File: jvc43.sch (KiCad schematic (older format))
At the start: 0 parts

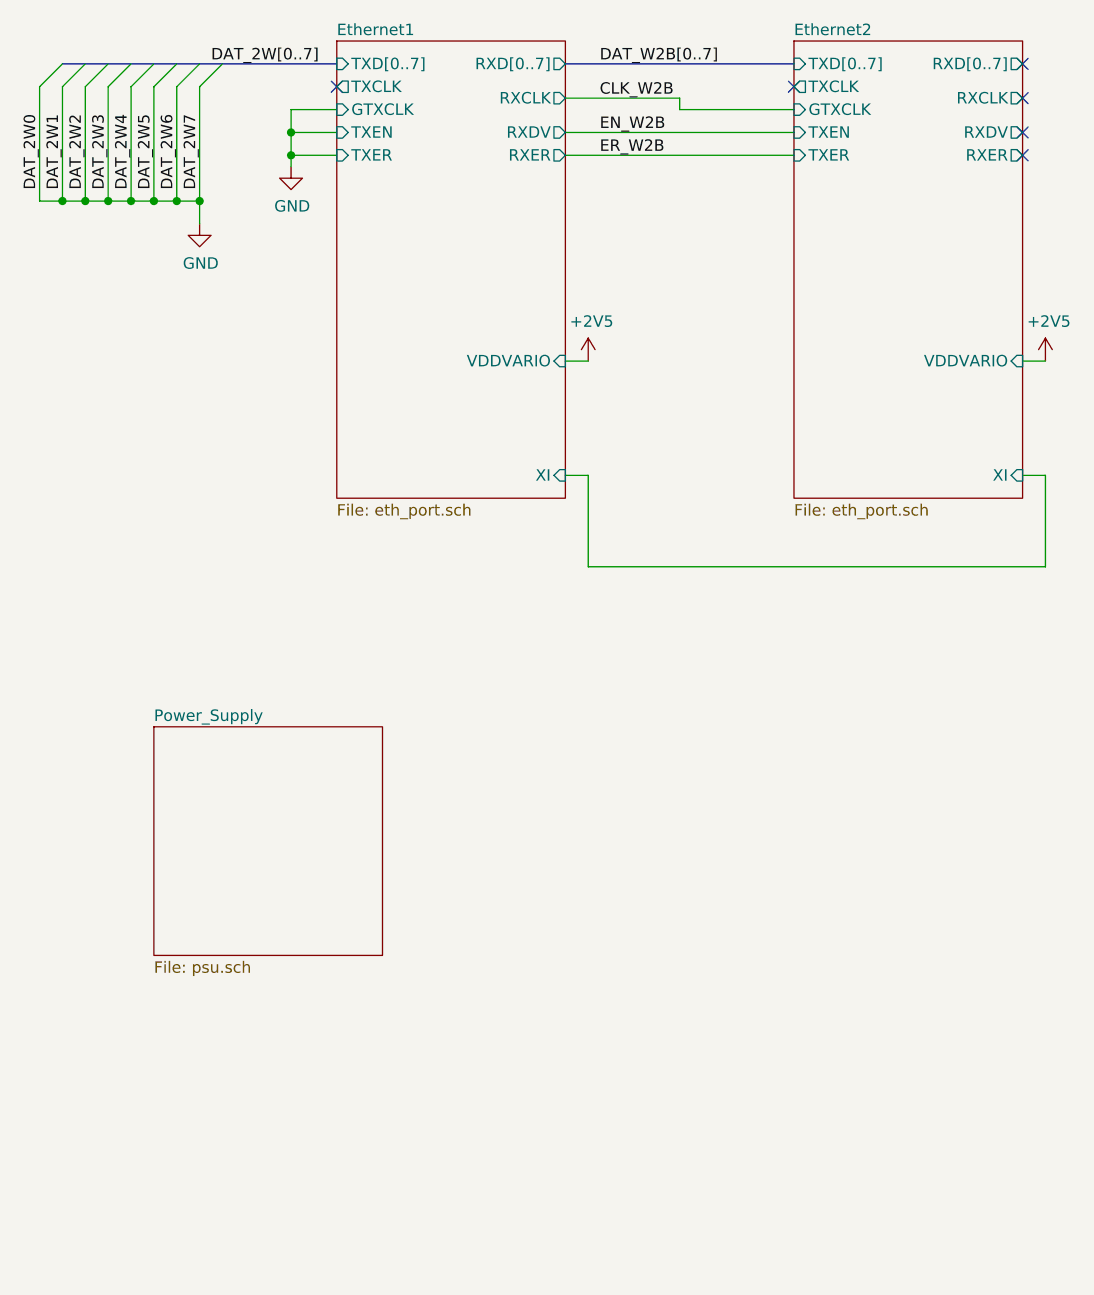
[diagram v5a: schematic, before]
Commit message: - Selected, schematic'd, placed & routed a crystal oscillator - Filled various internal planes to even out board thickness as well as   improve EMI performance - Added some identifying text to the top silkscreen
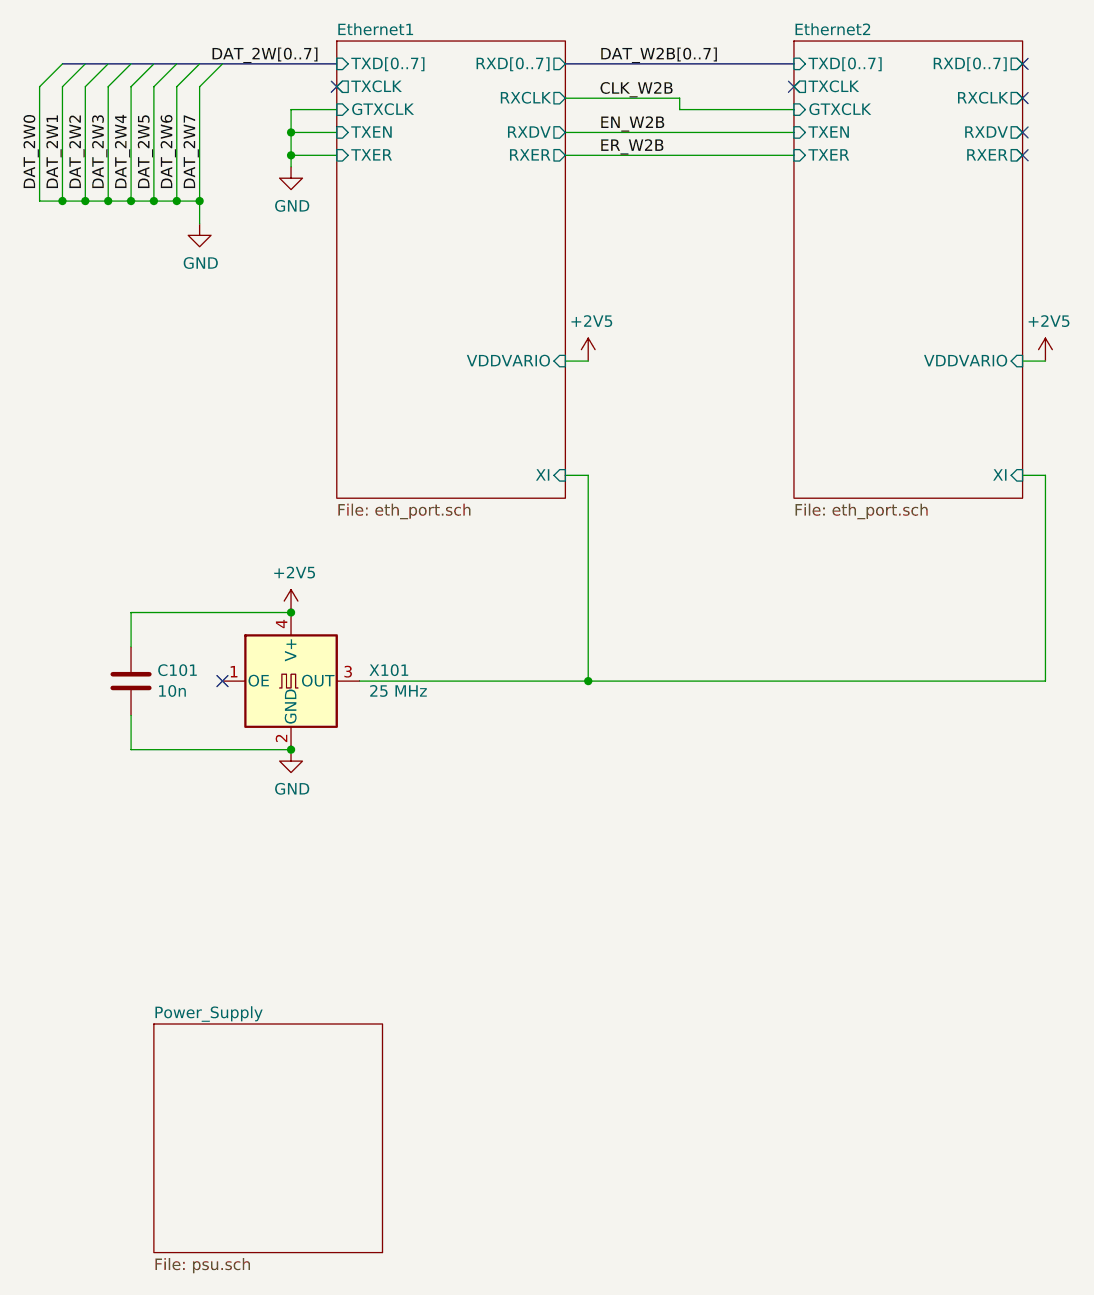
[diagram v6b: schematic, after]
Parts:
- added C101: 10n, Capacitor_SMD:C_0603_1608Metric, symbol Device:C
- added X101: 25 MHz, Crystal:Crystal_SMD_2520-4Pin_2.5x2.0mm, symbol Oscillator:SG-8002JA
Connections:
- net +2V5: now also C101.1, X101.4 (V+)
- net Ethernet1/XI: now also X101.3 (OUT)
- net GND: now also C101.2, X101.2 (GND)
- no-connect marks 6 -> 7
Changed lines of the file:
@@
 NoConn ~ 5800 1500
 $Sheet
-S 2000 4000 1000 1000
+S 2000 5300 1000 1000
 U 63912954
 F0 "Power_Supply" 50
@@
 	3800 2400 3900 2400
 $Comp
-L power:+2V5 #PWR?
+L power:+2V5 #PWR0103
 U 1 1 63A0D2C7
 P 3900 2400
-F 0 "#PWR?" H 3900 2250 50  0001 C CNN
+F 0 "#PWR0103" H 3900 2250 50  0001 C CNN
 F 1 "+2V5" H 3915 2573 50  0000 C CNN
 F 2 "" H 3900 2400 50  0001 C CNN
@@
 	5800 2400 5900 2400
 $Comp
-L power:+2V5 #PWR?
+L power:+2V5 #PWR0104
 U 1 1 63A0D2DA
 P 5900 2400
-F 0 "#PWR?" H 5900 2250 50  0001 C CNN
+F 0 "#PWR0104" H 5900 2250 50  0001 C CNN
 F 1 "+2V5" H 5915 2573 50  0000 C CNN
 F 2 "" H 5900 2400 50  0001 C CNN
@@
 	3800 2900 3900 2900
 Wire Wire Line
-	3900 2900 3900 3300
+	3900 2900 3900 3800
 Wire Wire Line
-	3900 3300 5900 3300
+	3900 3800 5900 3800
 Wire Wire Line
-	5900 3300 5900 2900
+	5900 3800 5900 2900
 Wire Wire Line
 	5900 2900 5800 2900
+$Comp
+L Oscillator:SG-8002JA X101
+U 1 1 6392A89E
+P 2600 3800
+F 0 "X101" H 2941 3846 50  0000 L CNN
+F 1 "25 MHz" H 2941 3755 50  0000 L CNN
+F 2 "Crystal:Crystal_SMD_2520-4Pin_2.5x2.0mm" H 3300 3450 50  0001 C CNN
+F 3 "~" H 2500 3800 50  0001 C CNN
+F 4 "ECS-2520MV-250-CN-TR" H 2600 3800 50  0001 C CNN "Part#"
+	1    2600 3800
+	1    0    0    -1
+$EndComp
+Wire Wire Line
+	3900 3800 2900 3800
+Connection ~ 3900 3800
+NoConn ~ 2300 3800
+$Comp
+L Device:C C101
+U 1 1 6392BD03
+P 1900 3800
+F 0 "C101" H 2015 3846 50  0000 L CNN
+F 1 "10n" H 2015 3755 50  0000 L CNN
+F 2 "Capacitor_SMD:C_0603_1608Metric" H 1938 3650 50  0001 C CNN
+F 3 "~" H 1900 3800 50  0001 C CNN
+F 4 "6.3V" H 1900 3800 50  0001 C CNN "Voltage"
+	1    1900 3800
+	1    0    0    -1
+$EndComp
+Wire Wire Line
+	1900 3950 1900 4100
+Wire Wire Line
+	1900 4100 2600 4100
+$Comp
+L power:GND #PWR0106
+U 1 1 6392C346
+P 2600 4100
+F 0 "#PWR0106" H 2600 3850 50  0001 C CNN
+F 1 "GND" H 2605 3927 50  0000 C CNN
+F 2 "" H 2600 4100 50  0001 C CNN
+F 3 "" H 2600 4100 50  0001 C CNN
+	1    2600 4100
+	1    0    0    -1
+$EndComp
+Connection ~ 2600 4100
+$Comp
+L power:+2V5 #PWR0105
+U 1 1 6392C398
+P 2600 3500
+F 0 "#PWR0105" H 2600 3350 50  0001 C CNN
+F 1 "+2V5" H 2615 3673 50  0000 C CNN
+F 2 "" H 2600 3500 50  0001 C CNN
+F 3 "" H 2600 3500 50  0001 C CNN
+	1    2600 3500
+	1    0    0    -1
+$EndComp
+Wire Wire Line
+	2600 3500 1900 3500
+Wire Wire Line
+	1900 3500 1900 3650
 Wire Bus Line
 	1600 1100 2800 1100
+Connection ~ 2600 3500
 $EndSCHEMATC
